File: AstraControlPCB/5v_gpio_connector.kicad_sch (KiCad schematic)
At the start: 1 part, among them CN9 4P JST VH

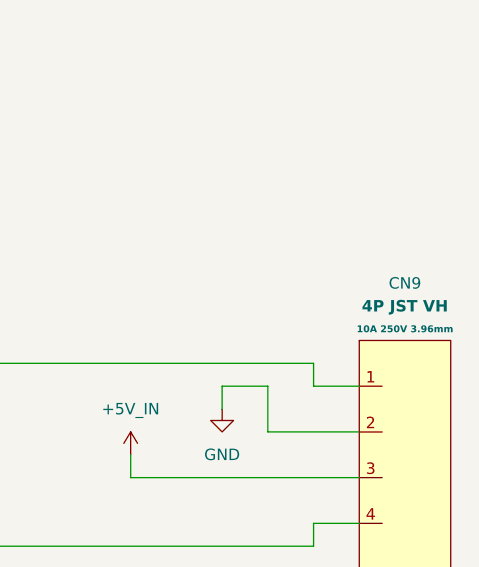
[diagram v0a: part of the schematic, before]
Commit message: New inductor that is in stock, updated rs485 ic layout to put caps closer
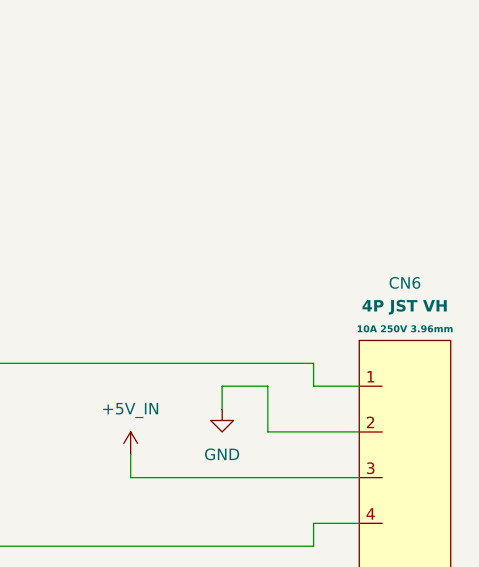
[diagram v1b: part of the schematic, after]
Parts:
- renumbered CN9 to CN6
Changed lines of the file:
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@@
 		(dnp no)
 		(fields_autoplaced yes)
-		(property "Reference" "#PWR095"
+		(property "Reference" "#PWR083"
 			(at 137.16 102.87 0)
 			(effects
@@
 			(project "AstraControl"
 				(path "/9a751838-dce8-4d69-8a02-736625ac74e7/0db21d8e-3390-4d67-877f-0e5d98e37848/62b5576a-8261-4301-b741-3feb86a98cd0"
-					(reference "#PWR095")
+					(reference "#PWR083")
 					(unit 1)
 				)
@@
 		(on_board yes)
 		(dnp no)
-		(property "Reference" "CN9"
+		(property "Reference" "CN6"
 			(at 157.48 82.55 0)
 			(effects
@@
 			(project "AstraControl"
 				(path "/9a751838-dce8-4d69-8a02-736625ac74e7/0db21d8e-3390-4d67-877f-0e5d98e37848/62b5576a-8261-4301-b741-3feb86a98cd0"
-					(reference "CN9")
+					(reference "CN6")
 					(unit 1)
 				)
@@
 		(dnp no)
 		(fields_autoplaced yes)
-		(property "Reference" "#PWR094"
+		(property "Reference" "#PWR082"
 			(at 127 105.41 0)
 			(effects
@@
 			(project "AstraControl"
 				(path "/9a751838-dce8-4d69-8a02-736625ac74e7/0db21d8e-3390-4d67-877f-0e5d98e37848/62b5576a-8261-4301-b741-3feb86a98cd0"
-					(reference "#PWR094")
+					(reference "#PWR082")
 					(unit 1)
 				)

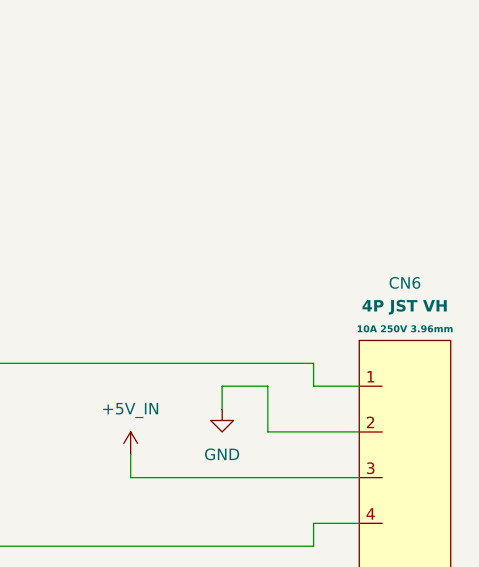
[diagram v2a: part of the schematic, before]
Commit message: Updated to JST SH, 3A diode for USB, added extra 2P VH
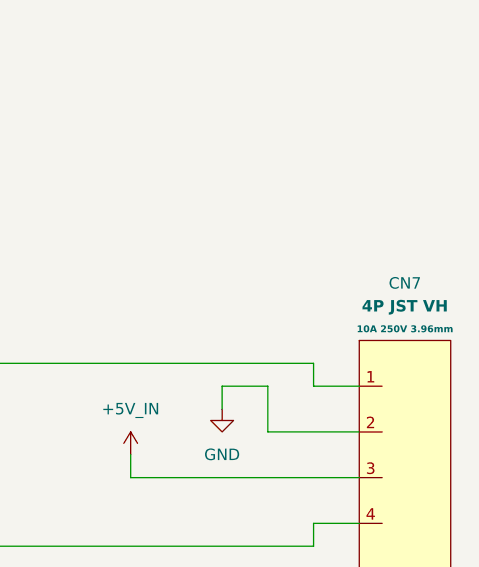
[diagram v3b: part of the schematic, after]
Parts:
- renumbered CN6 to CN7
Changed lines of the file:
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@@
 		(dnp no)
 		(fields_autoplaced yes)
-		(property "Reference" "#PWR082"
+		(property "Reference" "#PWR086"
 			(at 137.16 102.87 0)
 			(effects
@@
 			(project "AstraControl"
 				(path "/9a751838-dce8-4d69-8a02-736625ac74e7/0db21d8e-3390-4d67-877f-0e5d98e37848/62b5576a-8261-4301-b741-3feb86a98cd0"
-					(reference "#PWR082")
+					(reference "#PWR086")
 					(unit 1)
 				)
@@
 		(on_board yes)
 		(dnp no)
-		(property "Reference" "CN6"
+		(property "Reference" "CN7"
 			(at 157.48 82.55 0)
 			(effects
@@
 			(project "AstraControl"
 				(path "/9a751838-dce8-4d69-8a02-736625ac74e7/0db21d8e-3390-4d67-877f-0e5d98e37848/62b5576a-8261-4301-b741-3feb86a98cd0"
-					(reference "CN6")
+					(reference "CN7")
 					(unit 1)
 				)
@@
 		(dnp no)
 		(fields_autoplaced yes)
-		(property "Reference" "#PWR081"
+		(property "Reference" "#PWR085"
 			(at 127 105.41 0)
 			(effects
@@
 			(project "AstraControl"
 				(path "/9a751838-dce8-4d69-8a02-736625ac74e7/0db21d8e-3390-4d67-877f-0e5d98e37848/62b5576a-8261-4301-b741-3feb86a98cd0"
-					(reference "#PWR081")
+					(reference "#PWR085")
 					(unit 1)
 				)

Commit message: Update revision and add year to silkscreen
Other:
- title: AstraControl - 5V GPIO Connectors -> AstraControl - Root
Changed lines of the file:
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@@
 	(paper "A4")
 	(title_block
-		(title "AstraControl - 5V GPIO Connectors")
+		(title "AstraControl - Root")
 		(date "2024-08-26")
-		(rev "A")
+		(rev "B")
 		(company "LiveAstra Technologies")
 	)
